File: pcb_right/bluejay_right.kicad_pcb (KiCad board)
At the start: 2 copper layers, 147 x 140.5 mm, 69 parts, among them J2 SJ-43514, U2 MCP23017

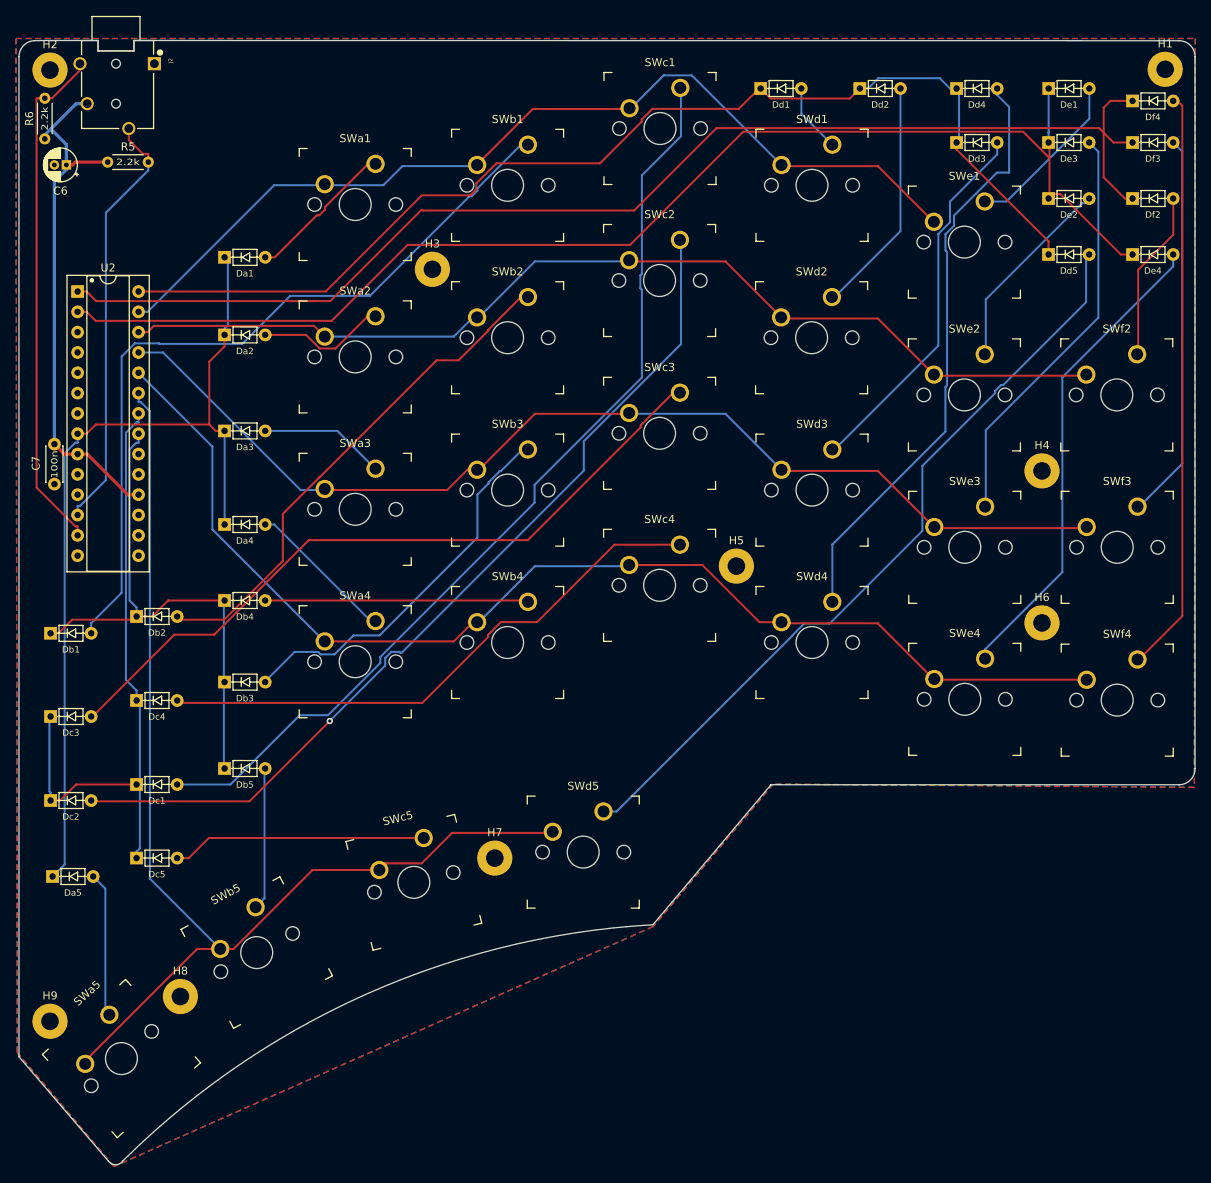
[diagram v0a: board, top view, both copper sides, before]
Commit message: Finish aligning switches, start work on plate
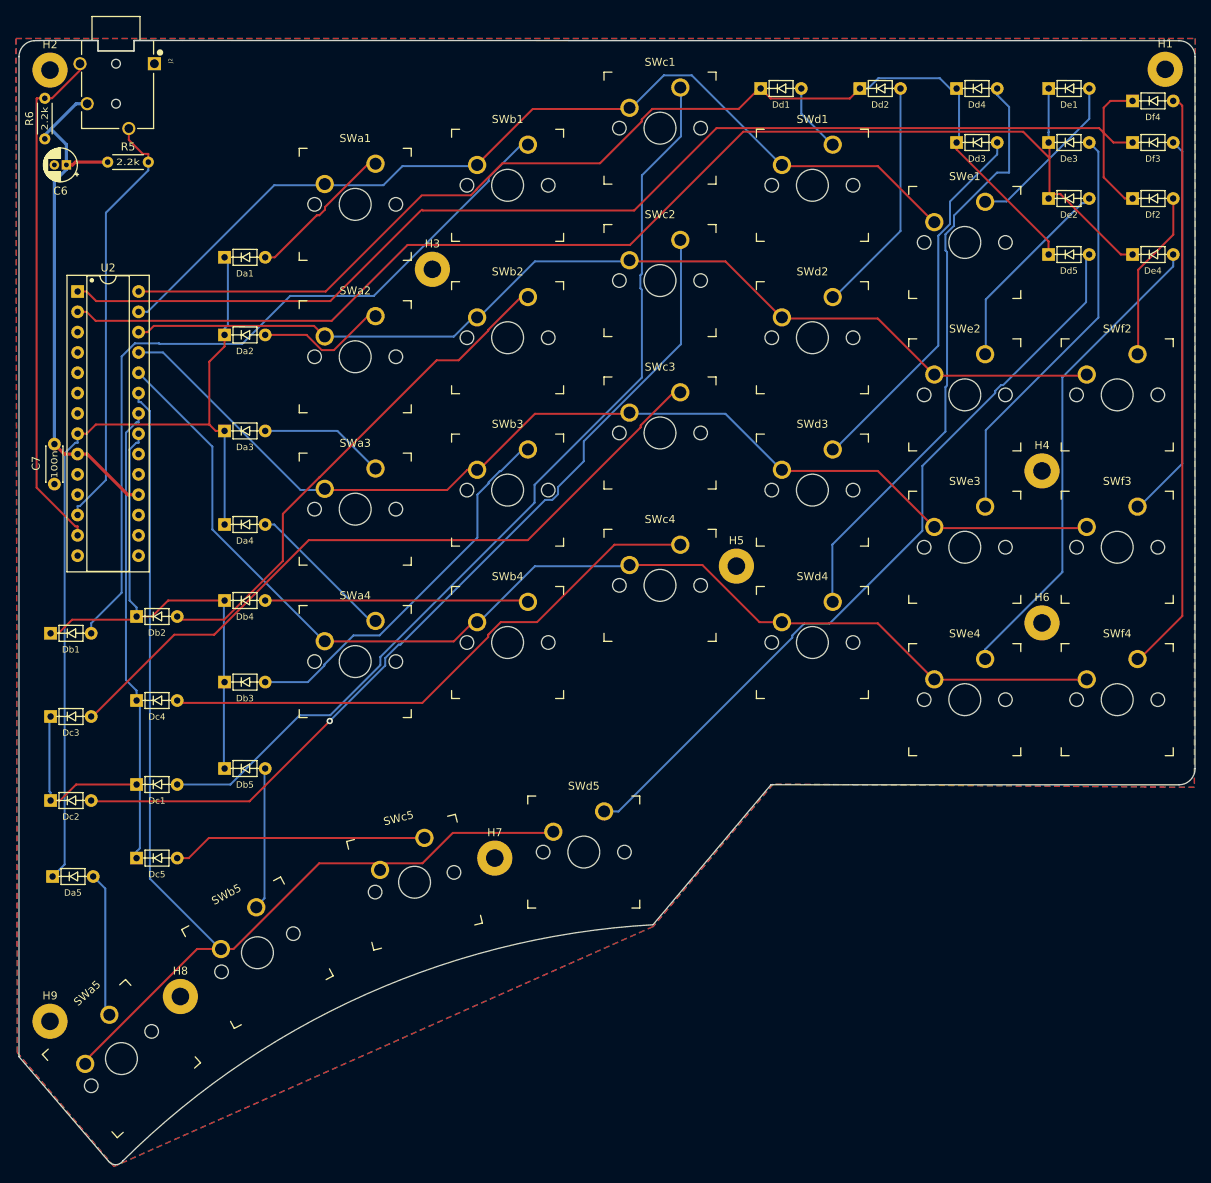
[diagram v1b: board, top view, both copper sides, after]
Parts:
- moved SWd2 0.10 mm to (38.1, -19.1)
- moved SWb5 0.09 mm to (-31.3, 57.8)
- moved SWc5 0.09 mm to (-11.6, 49.0)
- moved SWd5 0.08 mm to (9.53, 45.2)
- moved SWc3 0.07 mm to (19.1, -7.14)
- moved SWe1 0.07 mm to (57.1, -31.0)
- moved SWf4 0.06 mm to (76.2, 26.2)
- moved SWc4 0.05 mm to (19.1, 11.9)
- moved SWe2 0.05 mm to (57.1, -11.9)
- moved SWf2 0.05 mm to (76.2, -11.9)
- moved SWc2 0.05 mm to (19.1, -26.2)
- moved SWd1 0.05 mm to (38.1, -38.1)
- moved SWd3 0.05 mm to (38.1, 0.00)
- moved SWd4 0.05 mm to (38.1, 19.1)

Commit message: Ground a couple mounting holes so as to ground plate and base too
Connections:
- H2 pad 1: (no net) -> GND
- H3 pad 1: (no net) -> GND
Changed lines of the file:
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@@
     (property "Sheetfile" "bluejay_right.kicad_sch")
     (property "Sheetname" "")
-    (property "exclude_from_bom" "")
-    (attr exclude_from_pos_files exclude_from_bom)
+    (attr exclude_from_pos_files)
     (fp_text reference "H3" (at 0 -3.2) (layer "F.SilkS")
       (effects (font (size 1 1) (thickness 0.15)))
@@
     (fp_circle (center 0 0) (end 2.2 0) (layer "Cmts.User") (width 0.15) (fill none))
     (fp_circle (center 0 0) (end 2.45 0) (layer "F.CrtYd") (width 0.05) (fill none))
-    (pad "1" thru_hole circle (at 0 0) (size 4.4 4.4) (drill 2.2) (layers *.Cu *.Mask))
+    (pad "1" thru_hole circle (at 0 0) (size 4.4 4.4) (drill 2.2) (layers *.Cu *.Mask)
+      (net 2 "GND") (pinfunction "1") (pintype "input"))
   )
   (footprint "MountingHole:MountingHole_2.2mm_M2_Pad" (layer "F.Cu")
@@
     (property "Sheetfile" "bluejay_right.kicad_sch")
     (property "Sheetname" "")
-    (property "exclude_from_bom" "")
-    (attr exclude_from_pos_files exclude_from_bom)
+    (attr exclude_from_pos_files)
     (fp_text reference "H2" (at 0 -3.2) (layer "F.SilkS")
       (effects (font (size 1 1) (thickness 0.15)))
@@
     (fp_circle (center 0 0) (end 2.2 0) (layer "Cmts.User") (width 0.15) (fill none))
     (fp_circle (center 0 0) (end 2.45 0) (layer "F.CrtYd") (width 0.05) (fill none))
-    (pad "1" thru_hole circle (at 0 0) (size 4.4 4.4) (drill 2.2) (layers *.Cu *.Mask))
+    (pad "1" thru_hole circle (at 0 0) (size 4.4 4.4) (drill 2.2) (layers *.Cu *.Mask)
+      (net 2 "GND") (pinfunction "1") (pintype "input"))
   )
   (footprint "BlueJay footprints:D_DO-35_SOD27_P5.08mm_Horizontal" (layer "F.Cu")

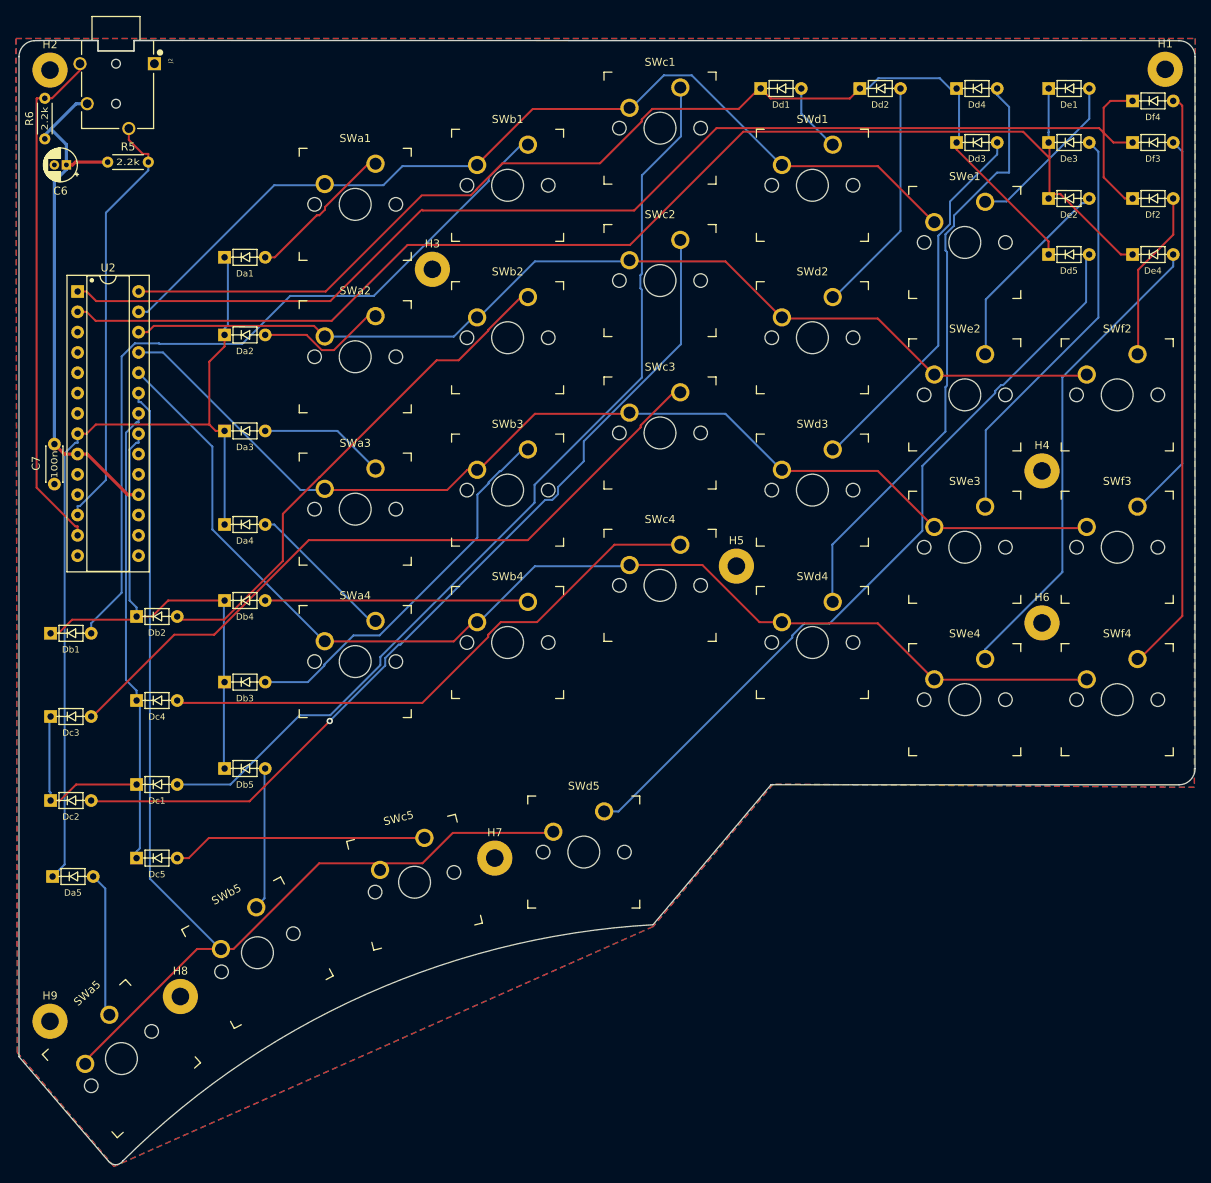
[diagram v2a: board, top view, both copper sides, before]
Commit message: Create base pcb
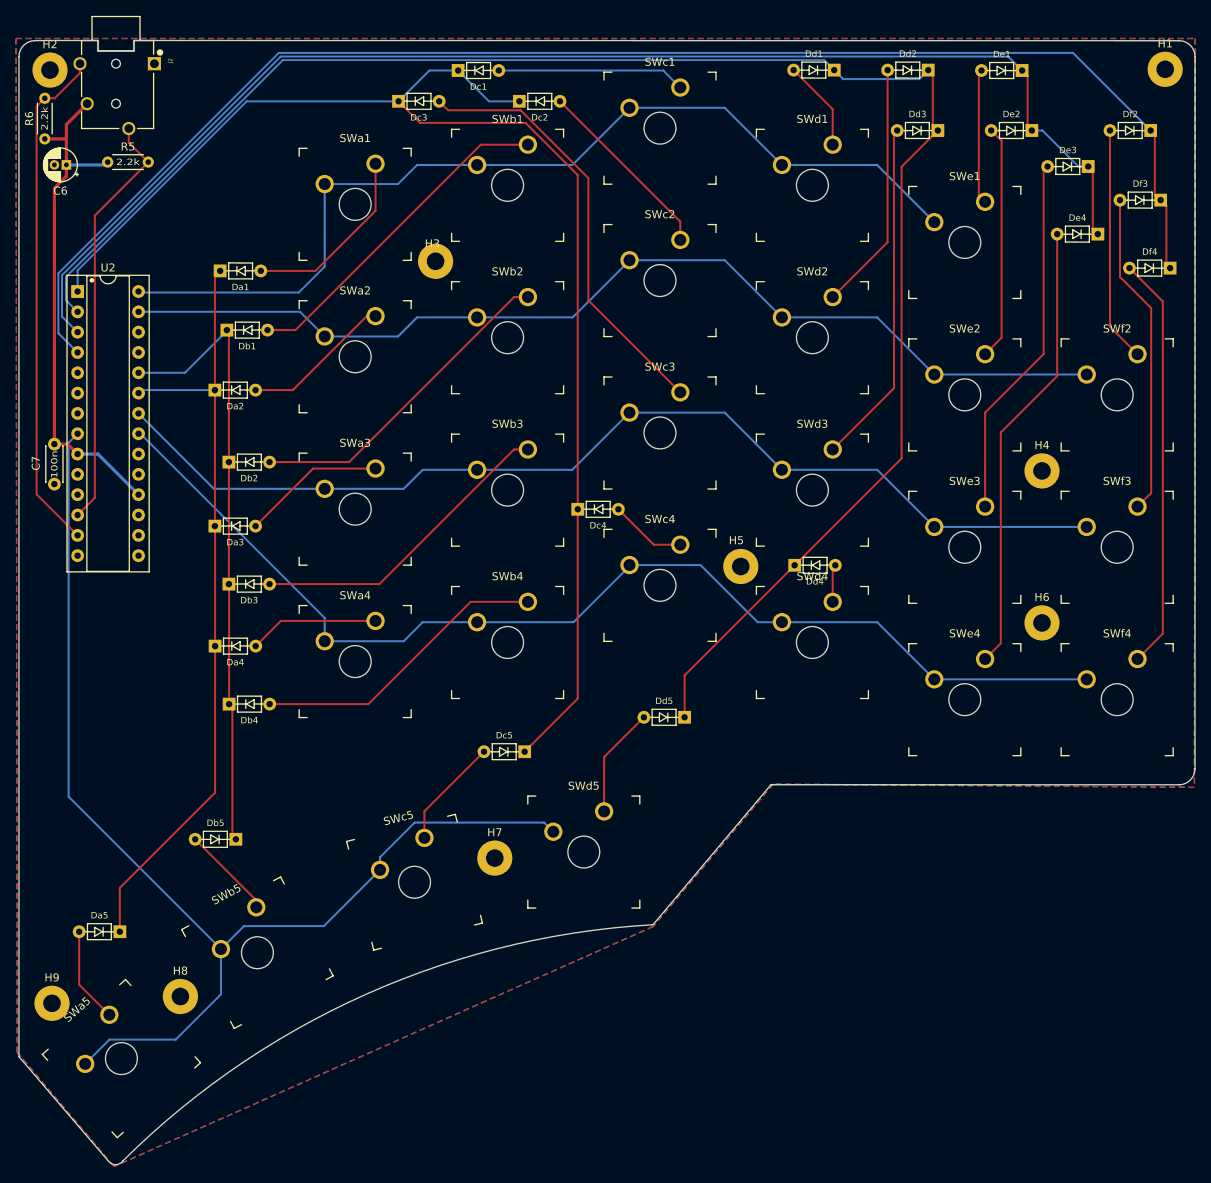
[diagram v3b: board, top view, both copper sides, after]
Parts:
- SWa1, SWa2, SWa3, SWa4, SWa5, SWb1, SWb2, SWb3, SWb4, SWb5, SWc1, SWc2, SWc3, SWc4, SWc5, SWd1, SWd2, SWd3, SWd4, SWd5, SWe1, SWe2, SWe3, SWe4, SWf2, SWf3, SWf4: footprint BlueJay footprints:SW_MX -> BlueJay footprints:SW_MX_Plate
- moved Dc2 105.2 mm to (0.20, -48.6)
- moved Dc1 97.9 mm to (-7.45, -52.5)
- moved Dc3 88.4 mm to (-14.9, -48.6)
- moved Dd5 72.1 mm to (23.4, 28.4), turned to 180 degrees
- moved Dd4 62.9 mm to (34.6, 9.40)
- moved Dc4 60.1 mm to (7.50, 2.40)
- moved Dc5 52.8 mm to (3.40, 32.7), turned to 180 degrees
- moved Db1 43.8 mm to (-36.4, -20.0)
- moved Db2 22.5 mm to (-36.1, -3.50)
- moved Df4 22.1 mm to (84.1, -27.8), turned to 180 degrees
- moved Da4 15.2 mm to (-37.8, 19.5)
- moved Db4 13.0 mm to (-36.1, 26.8)
- moved Da5 12.9 mm to (-47.2, 55.2), turned to 180 degrees
- moved Db3 12.3 mm to (-36.1, 11.8)
- moved Da3 12.0 mm to (-37.9, 4.50)
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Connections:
- U2 pad 1: /colF -> /colC
- U2 pad 2: /colE -> /colD
- U2 pad 21: /colB -> /row4
- U2 pad 22: /colC -> /row3
- U2 pad 23: /row5 -> /colA
- U2 pad 24: /row4 -> /colB
- U2 pad 25: /row3 -> unconnected-(U2-Pad25)
- U2 pad 26: /row2 -> unconnected-(U2-Pad26)
- U2 pad 27: /row1 -> /row2
- U2 pad 28: /colD -> /row1
- U2 pad 3: unconnected-(U2-Pad3) -> /colE
- U2 pad 4: unconnected-(U2-Pad4) -> /colF
- U2 pad 8: /colA -> /row5
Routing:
- net Net-(Dc1-Pad2): track 119.5 -> 23.6 mm
- net /colC: track 79.8 -> 170.9 mm
- net Net-(Dc2-Pad2): track 113.1 -> 23.6 mm, vias 1 -> 0
- net Net-(Dd5-Pad2): track 97.9 -> 13.8 mm
- net /colD: track 140.7 -> 220.6 mm
- net Net-(Dd4-Pad2): track 75.0 -> 4.70 mm
- net Net-(Dc4-Pad2): track 71.3 -> 9.57 mm
- net Net-(Db1-Pad2): track 98.2 -> 42.1 mm
- net Net-(Dc3-Pad2): track 90.5 -> 54.2 mm
- net Net-(Db2-Pad2): track 64.2 -> 40.8 mm
- net /colF: track 159.3 -> 181.1 mm
- net Net-(Df4-Pad2): track 73.0 -> 51.9 mm
- net Net-(Dc5-Pad2): track 31.9 -> 13.9 mm
- net /colA: track 109.7 -> 97.5 mm
- net /colB: track 68.4 -> 77.4 mm
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
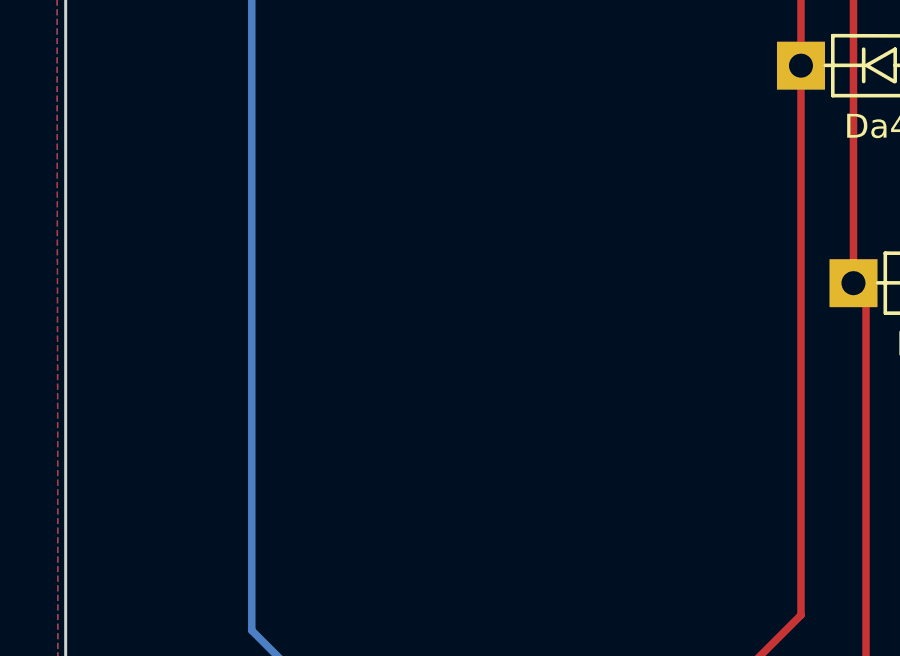
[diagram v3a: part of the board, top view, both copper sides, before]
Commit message: add logo
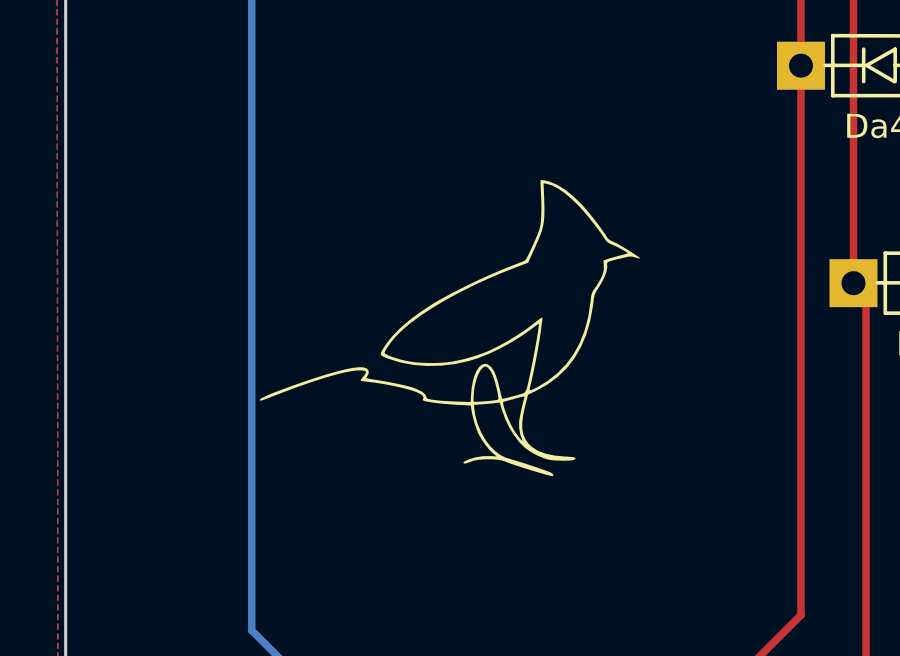
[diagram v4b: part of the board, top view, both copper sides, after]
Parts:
- added G***: LOGO, BlueJay footprints:bluejay_logo_small, F.Cu at (-48.2, 28.2)

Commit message: work on plate
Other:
- board text added: "JLCJLCJLCJLC"
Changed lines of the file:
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@@
   (gr_line (start -61.077843 -54.17) (end -61.077844 70.83) (layer "Edge.Cuts") (width 0.1))
   (gr_arc (start 83.927845 -56.17) (mid 85.346087 -55.593736) (end 85.927845 -54.17775) (layer "Edge.Cuts") (width 0.1))
+  (gr_text "JLCJLCJLCJLC" (at 79.63 35.43) (layer "B.Cu")
+    (effects (font (size 1 1) (thickness 0.2)) (justify mirror))
+  )
   (segment (start -55.15 -39.25) (end -55.15 -40.65) (width 0.4) (layer "F.Cu") (net 1))
   (segment (start -57.85 -43.9) (end -55.2 -43.9) (width 0.4) (layer "F.Cu") (net 1))
